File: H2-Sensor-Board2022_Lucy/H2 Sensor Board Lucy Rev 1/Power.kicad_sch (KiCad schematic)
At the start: 44 parts, among them J2 Conn_02x03_Top_Bottom, Q1 NMOS, U3 AZ1117H-5.0, U4 TPS2596, U6 AZ1117EH-3.3

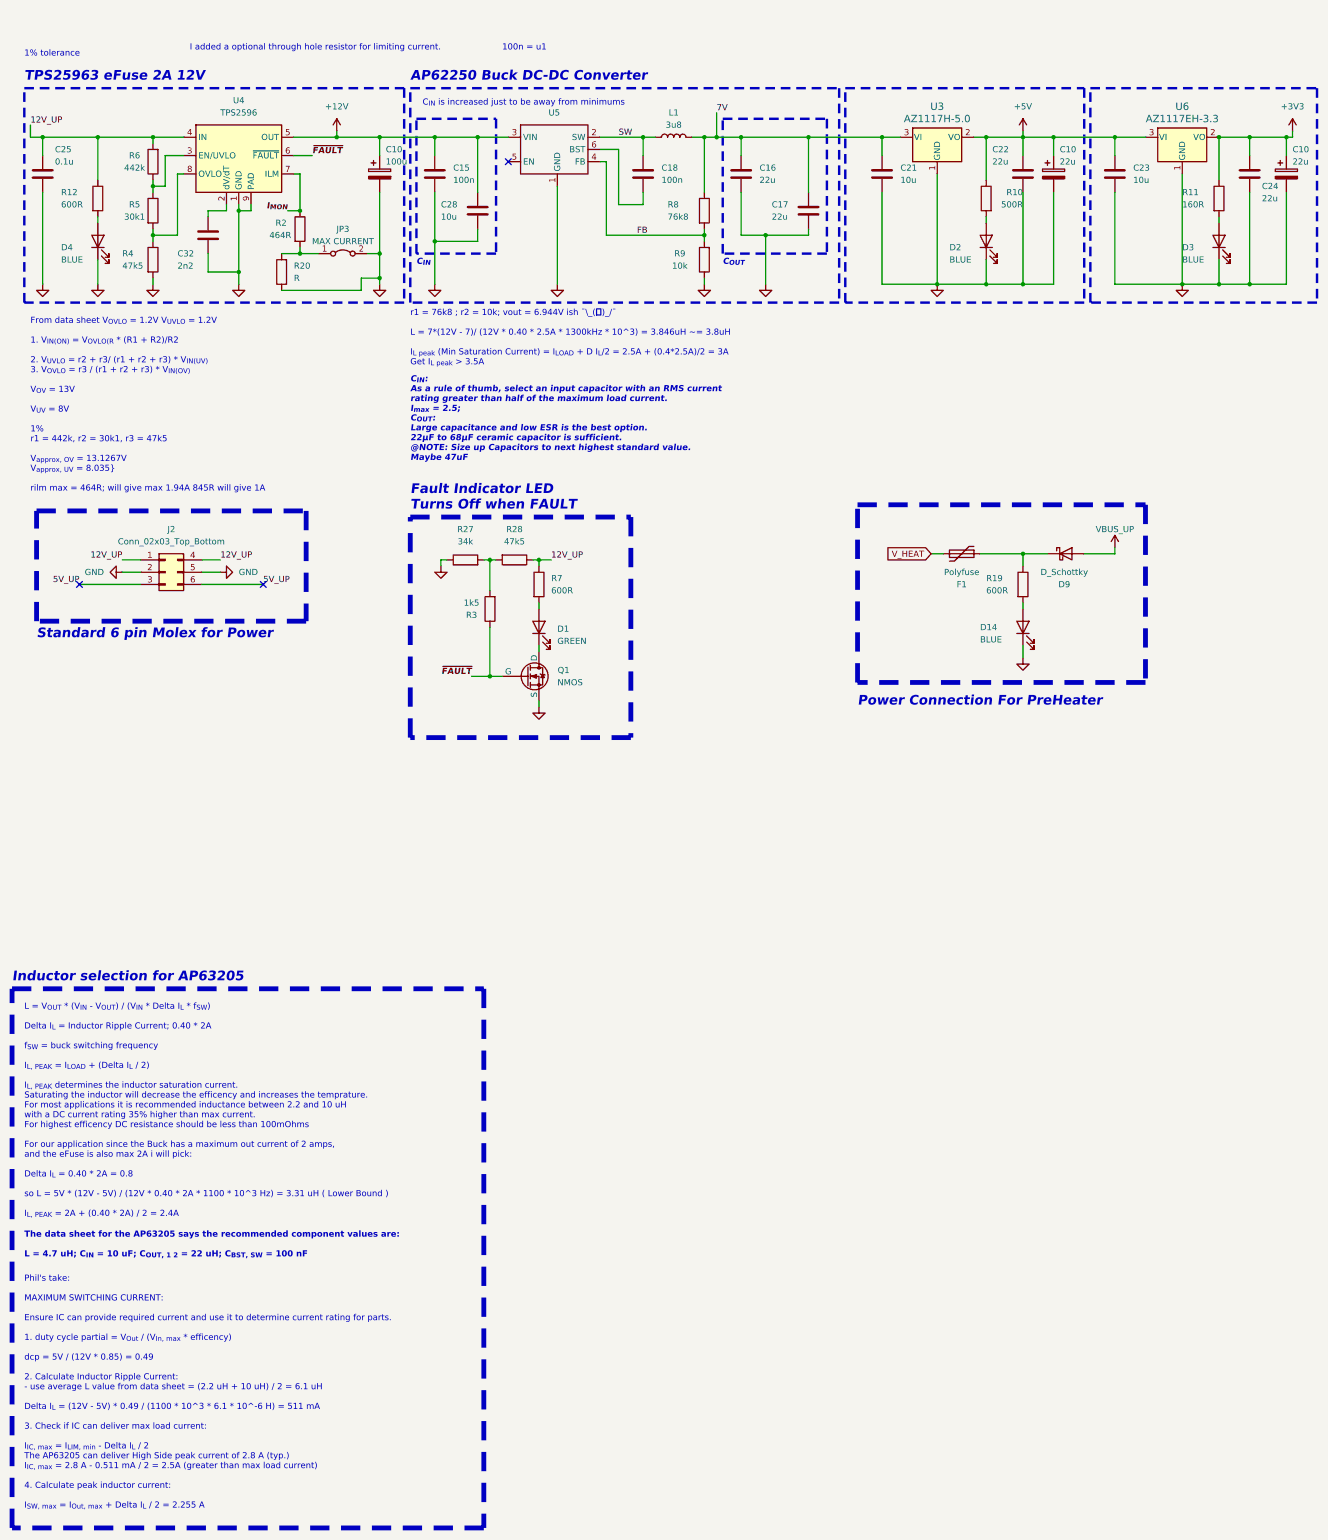
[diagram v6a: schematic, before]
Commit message: added inductor
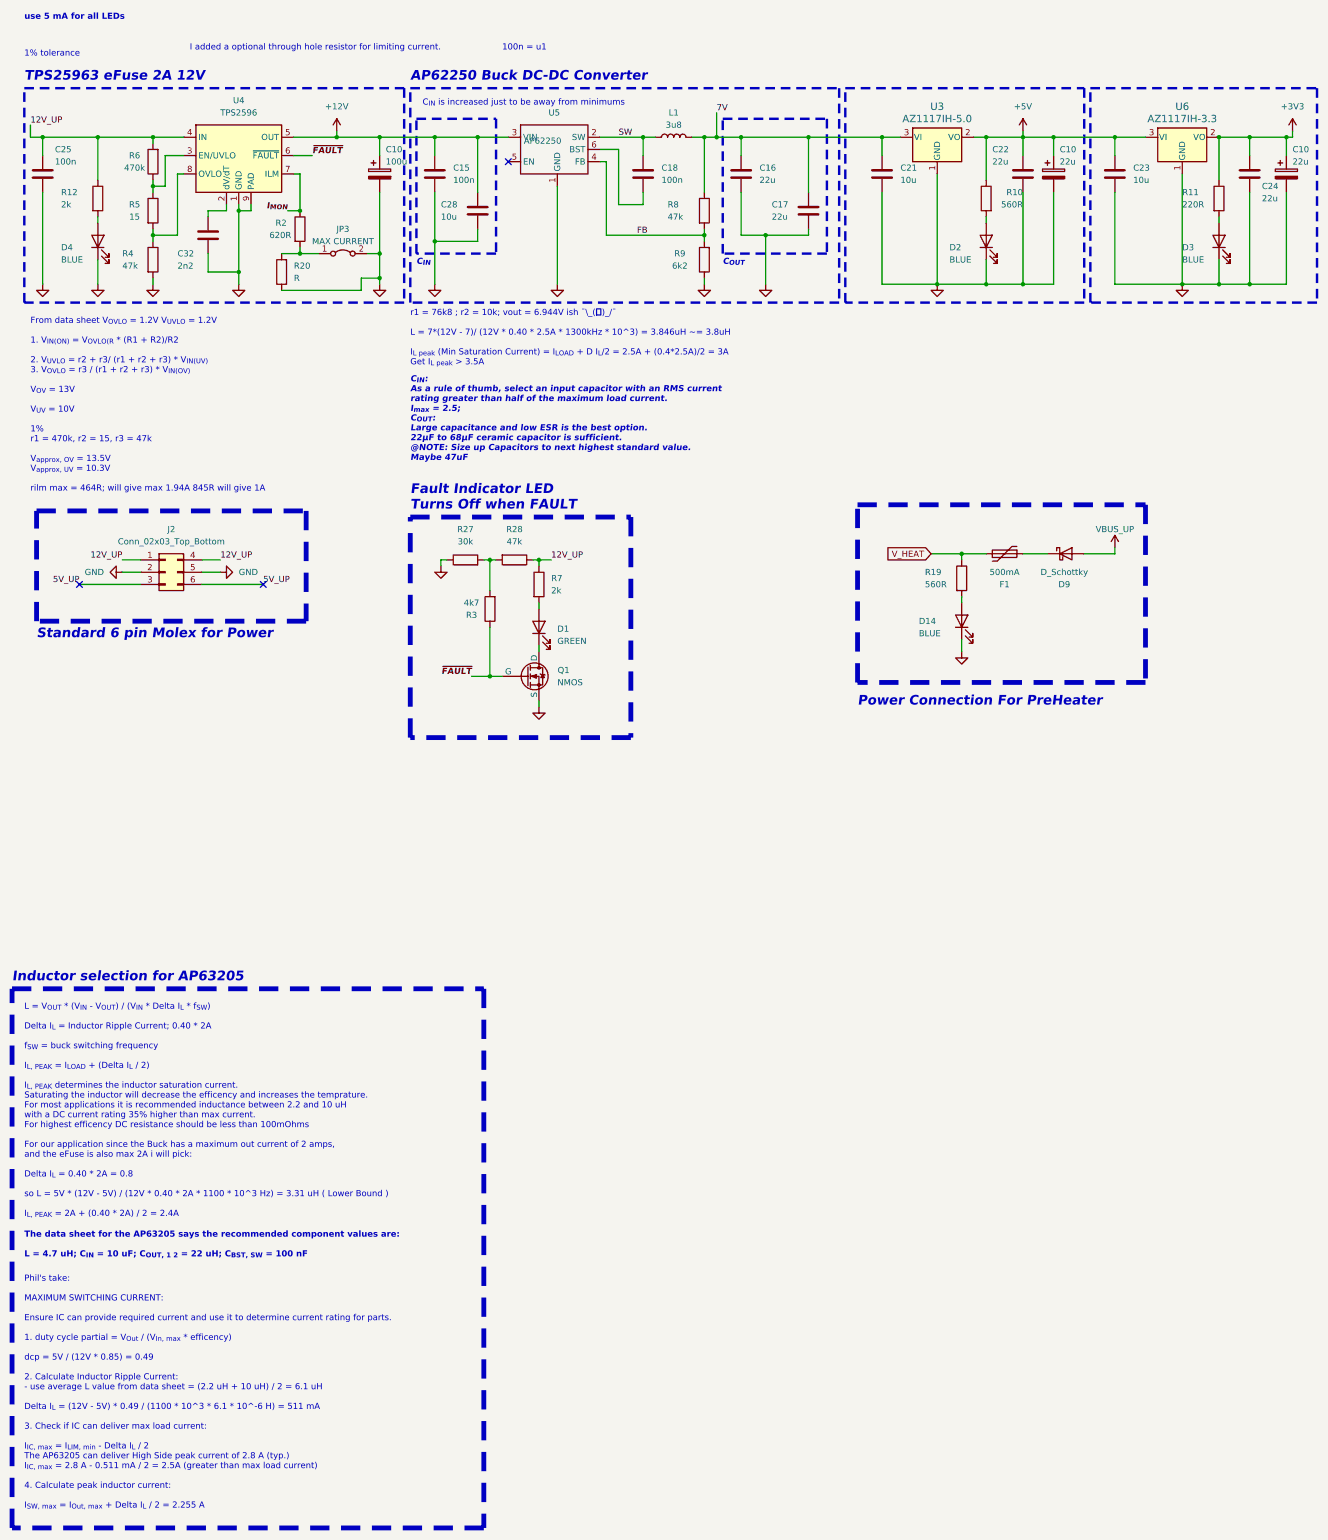
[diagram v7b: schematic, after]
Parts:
- C10: DK # 732-13321-1-ND -> 399-A766EB226M1DLAE060CT-ND
- C15, C18: JLCPCB Part#(Optional) C1525 -> C14663; JLCPCB Part#(optional) (none) -> C14663
- C16, C17: DK # (none) -> 1276-1851-1-ND
- C21, C23: JLCPCB Part#(Optional) (none) -> C440198; JLCPCB Part#(optional) (none) -> C440198
- C22, C24: JLCPCB Part#(Optional) (none) -> C45783; JLCPCB Part#(optional) (none) -> C45783
- C25: value 0.1u -> 100n; JLCPCB Part#(Optional) (none) -> C28233; JLCPCB Part#(optional) (none) -> C49678
- C28: DK # (none) -> 1276-1854-1-ND; JLCPCB Part#(optional) (none) -> -- mixed values --
- C32: JLCPCB Part#(Optional) (none) -> C1531; JLCPCB Part#(optional) (none) -> C1531
- D1: JLCPCB Part#(Optional) (none) -> C2297; JLCPCB Part#(optional) (none) -> C2297
- F1: value Polyfuse -> 500mA; footprint Fuse:Fuse_1206_3216Metric -> Fuse:Fuse_0805_2012Metric; DK # (none) -> 507-1811-1-ND
- L1: DK # (none) -> CDRH125L125NP-3R9NC
- Q1: JLCPCB Part#(Optional) (none) -> C8545; JLCPCB Part#(optional) (none) -> C8545
- R10: value 500R -> 560R; JLCPCB Part#(Optional) (none) -> C28636; JLCPCB Part#(optional) (none) -> C28636
- R11: value 160R -> 220R; JLCPCB Part#(Optional) (none) -> C17557; JLCPCB Part#(optional) (none) -> C17557
- R12, R7: value 600R -> 2k; JLCPCB Part#(Optional) (none) -> C17604; JLCPCB Part#(optional) (none) -> C17604
- R19: value 600R -> 560R; JLCPCB Part#(Optional) (none) -> C28636; JLCPCB Part#(optional) (none) -> C28636
- R2: value 464R -> 620R; footprint Resistor_SMD:R_0805_2012Metric -> Resistor_SMD:R_0603_1608Metric; JLCPCB Part#(Optional) (none) -> C23220; JLCPCB Part#(optional) (none) -> C23220
- R27: value 34k -> 30k; JLCPCB Part#(Optional) (none) -> C22984; JLCPCB Part#(optional) (none) -> C22984
- R28: value 47k5 -> 47k; JLCPCB Part#(Optional) (none) -> C25819; JLCPCB Part#(optional) (none) -> C25819
- R3: value 1k5 -> 4k7; JLCPCB Part#(Optional) (none) -> C23162; JLCPCB Part#(optional) (none) -> C23162
- R4: value 47k5 -> 47k; JLCPCB Part#(optional) (none) -> C17713
- R5: value 30k1 -> 15; JLCPCB Part#(optional) (none) -> C17480
- R6: value 442k -> 470k; JLCPCB Part#(optional) (none) -> C17709
- R8: value 76k8 -> 47k; JLCPCB Part#(Optional) (none) -> C17713; JLCPCB Part#(optional) (none) -> C17713
- R9: value 10k -> 6k2; JLCPCB Part#(Optional) (none) -> C17767; JLCPCB Part#(optional) (none) -> C17767
- U3: value AZ1117H-5.0 -> AZ1117IH-5.0; DK # (none) -> AZ1117IH-5.0TRG1DICT-ND; LCSC # C99343 -> (none)
- U4: DK # (none) -> 296-TPS259631DDARCT-ND; LCSC # C2155776 -> (none)
- U5: value ~ -> AP62250; DK # (none) -> 31-AP62250WU-7CT-ND
- U6: value AZ1117EH-3.3 -> AZ1117IH-3.3; DK # (none) -> AZ1117IH-3.3TRG1DICT-ND; LCSC # C108494 -> (none)
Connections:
- net V_HEAT: now also R19.1
- net at D9.1 (K), F1.1: no longer R19.1
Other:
- note added: "From data sheet V_{OVLO} = 1.2V V_{UVLO} = 1.2V 1. V_{IN(ON)} = V_{OVLO(R} * (R1 + R2)/R2 2. V_{UVLO} = r2 + r3/ (r1 + r2 + r3) * V_{IN(UV)} 3. V_{OVLO} = r3 / (r1 + r2 + r3) * V_{IN(OV)} V_{OV} = 13V V_{UV} = 10V 1% r1 = 470k, r2 = 15, r3 = 47k V_{approx, OV} = 13.5V V_{approx, UV} = 10.3V rilm max = 464R; will give max 1.94A 845R will give 1A"
- note added: "use 5 mA for all LEDs"
- note removed: "From data sheet V_{OVLO} = 1.2V V_{UVLO} = 1.2V 1. V_{IN(ON)} = V_{OVLO(R} * (R1 + R2)/R2 2. V_{UVLO} = r2 + r3/ (r1 + r2 + r3) * V_{IN(UV)} 3. V_{OVLO} = r3 / (r1 + r2 + r3) * V_{IN(OV)} V_{OV} = 13V V_{UV} = 8V 1% r1 = 442k, r2 = 30k1, r3 = 47k5 V_{approx, OV} = 13.1267V V_{approx, UV} = 8.035} rilm max = 464R; will give max 1.94A 845R will give 1A"
- moved on the sheet: D14, F1, R19

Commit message: doN:
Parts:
- C16, C17: DK # 1276-1851-1-ND -> 1276-1101-1-ND
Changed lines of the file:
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@@
       (effects (font (size 1.27 1.27)) hide)
     )
-    (property "DK #" "1276-1851-1-ND" (at 162.56 48.26 0)
+    (property "DK #" "1276-1101-1-ND" (at 162.56 48.26 0)
       (effects (font (size 1.27 1.27)) hide)
     )
@@
       (effects (font (size 1.27 1.27)) hide)
     )
-    (property "DK #" "1276-1851-1-ND" (at 176.53 55.88 0)
-      (effects (font (size 1.27 1.27)) hide)
-    )
+    (property "DK #" "1276-1101-1-ND" (at 176.53 55.88 0)
+      (effects (font (size 1.27 1.27)) hide)
+    )
